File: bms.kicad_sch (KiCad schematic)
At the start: 95 parts, among them J1 Conn_01x13, J2 SWD, J3 I2C_IN, J4 I2C_OUT, SW1 SW_Push, U1 LMR51610, U2 STM32F103C8Tx, U3 MAX14920, U4 MAX11163, U5 MAX6126, U6 ADuM1252, Y1 8M

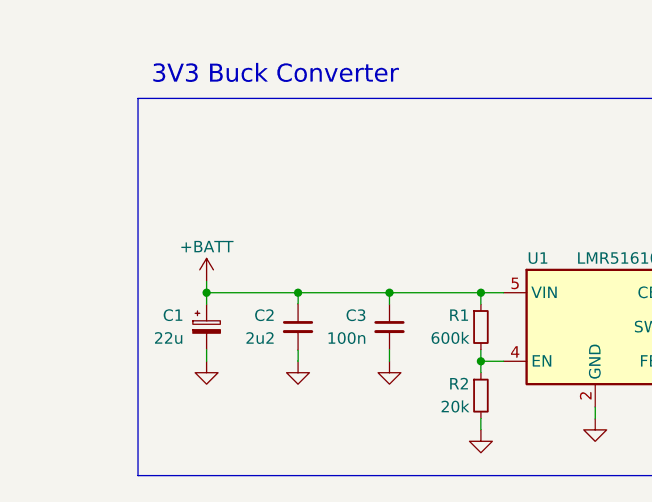
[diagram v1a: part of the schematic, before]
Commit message: schematic: Add input polyfuse
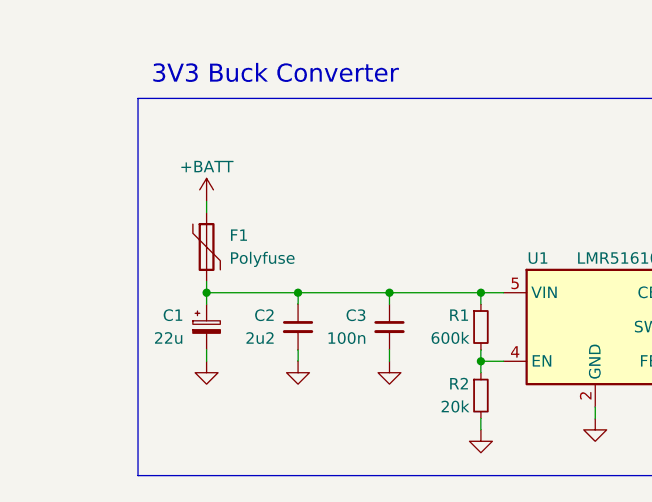
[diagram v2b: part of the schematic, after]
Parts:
- added F1: Polyfuse, Resistor_SMD:R_1206_3216Metric, symbol Device:Polyfuse
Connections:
- net +BATT: now also F1.1; no longer C1.1, C2.1, C3.1, R1.1, U1.5 (VIN)
- new net: C1.1, C2.1, C3.1, F1.2, R1.1, U1.5 (VIN)
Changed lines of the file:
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@@
 	(wire
 		(pts
+			(xy 33.02 35.56) (xy 33.02 36.83)
+		)
+		(stroke
+			(width 0)
+			(type default)
+		)
+	)
+	(wire
+		(pts
 			(xy 256.54 72.39) (xy 256.54 73.66)
 		)
@@
 	)
 	(symbol
+		(lib_id "Device:Polyfuse")
+		(at 33.02 40.64 0)
+		(unit 1)
+		(exclude_from_sim no)
+		(in_bom yes)
+		(on_board yes)
+		(dnp no)
+		(fields_autoplaced yes)
+		(property "Reference" "F1"
+			(at 35.56 39.3699 0)
+			(effects
+				(font
+					(size 1.27 1.27)
+				)
+				(justify left)
+			)
+		)
+		(property "Value" "Polyfuse"
+			(at 35.56 41.9099 0)
+			(effects
+				(font
+					(size 1.27 1.27)
+				)
+				(justify left)
+			)
+		)
+		(property "Footprint" "Resistor_SMD:R_1206_3216Metric"
+			(at 34.29 45.72 0)
+			(effects
+				(font
+					(size 1.27 1.27)
+				)
+				(justify left)
+				(hide yes)
+			)
+		)
+		(property "Datasheet" "~"
+			(at 33.02 40.64 0)
+			(effects
+				(font
+					(size 1.27 1.27)
+				)
+				(hide yes)
+			)
+		)
+		(property "Description" "Resettable fuse, polymeric positive temperature coefficient"
+			(at 33.02 40.64 0)
+			(effects
+				(font
+					(size 1.27 1.27)
+				)
+				(hide yes)
+			)
+		)
+		(property "Part Number" "1206L010/60WR"
+			(at 33.02 40.64 0)
+			(effects
+				(font
+					(size 1.27 1.27)
+				)
+				(hide yes)
+			)
+		)
+		(property "Role" "Input polyfuse"
+			(at 33.02 40.64 0)
+			(effects
+				(font
+					(size 1.27 1.27)
+				)
+				(hide yes)
+			)
+		)
+		(pin "1"
+		)
+		(pin "2"
+		)
+		(instances
+			(project ""
+				(path "/ae4a7653-8e6d-4e05-b144-1e5e3b2092b7"
+					(reference "F1")
+					(unit 1)
+				)
+			)
+		)
+	)
+	(symbol
 		(lib_id "power:GND")
 		(at 121.92 60.96 0)
@@
 	(symbol
 		(lib_id "power:+BATT")
-		(at 33.02 44.45 0)
+		(at 33.02 35.56 0)
 		(unit 1)
 		(exclude_from_sim no)
@@
 		(dnp no)
 		(property "Reference" "#PWR03"
-			(at 33.02 48.26 0)
+			(at 33.02 39.37 0)
 			(effects
 				(font
@@
 		)
 		(property "Value" "+BATT"
-			(at 33.02 40.64 0)
+			(at 33.02 31.75 0)
 			(effects
 				(font
@@
 		)
 		(property "Footprint" ""
-			(at 33.02 44.45 0)
+			(at 33.02 35.56 0)
 			(effects
 				(font
@@
 		)
 		(property "Datasheet" ""
-			(at 33.02 44.45 0)
+			(at 33.02 35.56 0)
 			(effects
 				(font
@@
 		)
 		(property "Description" "Power symbol creates a global label with name \"+BATT\""
-			(at 33.02 44.45 0)
+			(at 33.02 35.56 0)
 			(effects
 				(font

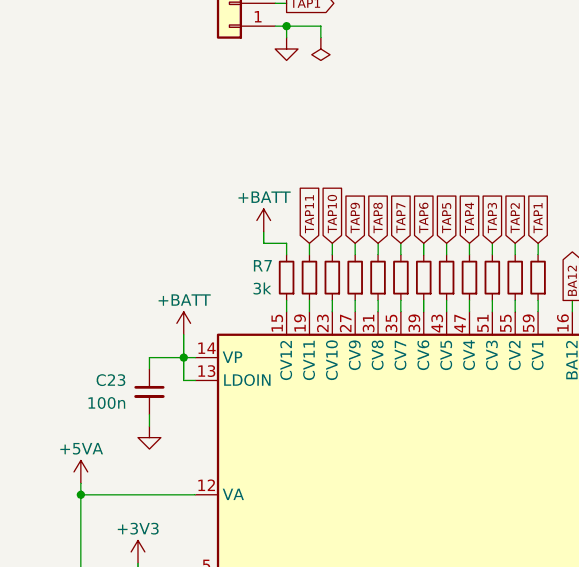
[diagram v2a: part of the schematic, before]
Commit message: schematic: Add resistor to MAX14920 input
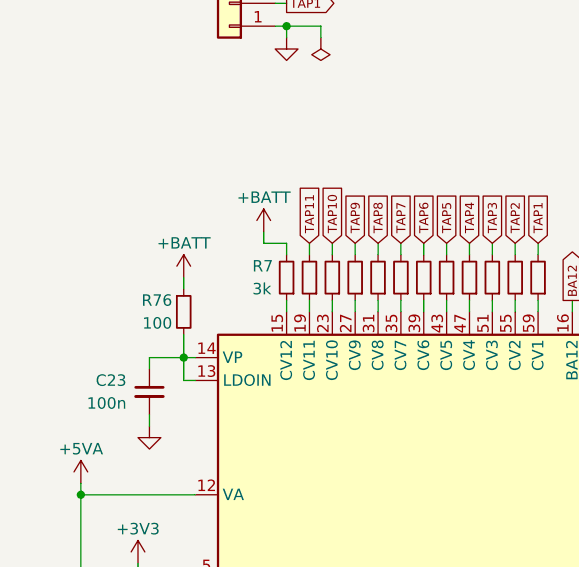
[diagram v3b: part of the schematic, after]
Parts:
- added R76: 100, Resistor_SMD:R_0603_1608Metric, symbol Device:R_Small
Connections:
- net +BATT: now also R76.1; no longer C23.1, U3.13 (LDOIN), U3.14 (VP)
- new net: C23.1, R76.2, U3.13 (LDOIN), U3.14 (VP)
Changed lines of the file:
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@@
 	(wire
 		(pts
+			(xy 30.48 137.16) (xy 30.48 138.43)
+		)
+		(stroke
+			(width 0)
+			(type default)
+		)
+	)
+	(wire
+		(pts
 			(xy 106.68 138.43) (xy 107.95 138.43)
 		)
@@
 	(symbol
 		(lib_id "power:+BATT")
-		(at 30.48 143.51 0)
+		(at 30.48 137.16 0)
 		(unit 1)
 		(exclude_from_sim no)
@@
 		(dnp no)
 		(property "Reference" "#PWR025"
-			(at 30.48 147.32 0)
+			(at 30.48 140.97 0)
 			(effects
 				(font
@@
 		)
 		(property "Value" "+BATT"
-			(at 30.48 139.7 0)
+			(at 30.48 133.35 0)
 			(effects
 				(font
@@
 		)
 		(property "Footprint" ""
-			(at 30.48 143.51 0)
+			(at 30.48 137.16 0)
 			(effects
 				(font
@@
 		)
 		(property "Datasheet" ""
-			(at 30.48 143.51 0)
+			(at 30.48 137.16 0)
 			(effects
 				(font
@@
 		)
 		(property "Description" "Power symbol creates a global label with name \"+BATT\""
-			(at 30.48 143.51 0)
+			(at 30.48 137.16 0)
 			(effects
 				(font
@@
 					(unit 1)
 				)
+			)
+		)
+	)
+	(symbol
+		(lib_id "Device:R_Small")
+		(at 30.48 140.97 0)
+		(unit 1)
+		(exclude_from_sim no)
+		(in_bom yes)
+		(on_board yes)
+		(dnp no)
+		(property "Reference" "R76"
+			(at 29.21 139.7 0)
+			(effects
+				(font
+					(size 1.27 1.27)
+				)
+				(justify right)
+			)
+		)
+		(property "Value" "100"
+			(at 29.21 142.24 0)
+			(effects
+				(font
+					(size 1.27 1.27)
+				)
+				(justify right)
+			)
+		)
+		(property "Footprint" "Resistor_SMD:R_0603_1608Metric"
+			(at 30.48 140.97 0)
+			(effects
+				(font
+					(size 1.27 1.27)
+				)
+				(hide yes)
+			)
+		)
+		(property "Datasheet" "~"
+			(at 30.48 140.97 0)
+			(effects
+				(font
+					(size 1.27 1.27)
+				)
+				(hide yes)
+			)
+		)
+		(property "Description" "Resistor, small symbol"
+			(at 30.48 140.97 0)
+			(effects
+				(font
+					(size 1.27 1.27)
+				)
+				(hide yes)
+			)
+		)
+		(property "Role" "MAX14920 inrush limit"
+			(at 30.48 140.97 0)
+			(effects
+				(font
+					(size 1.27 1.27)
+				)
+				(hide yes)
+			)
+		)
+		(pin "1"
+		)
+		(pin "2"
+		)
+		(instances
+			(project ""
+				(path "/ae4a7653-8e6d-4e05-b144-1e5e3b2092b7"
+					(reference "R76")
+					(unit 1)
+				)

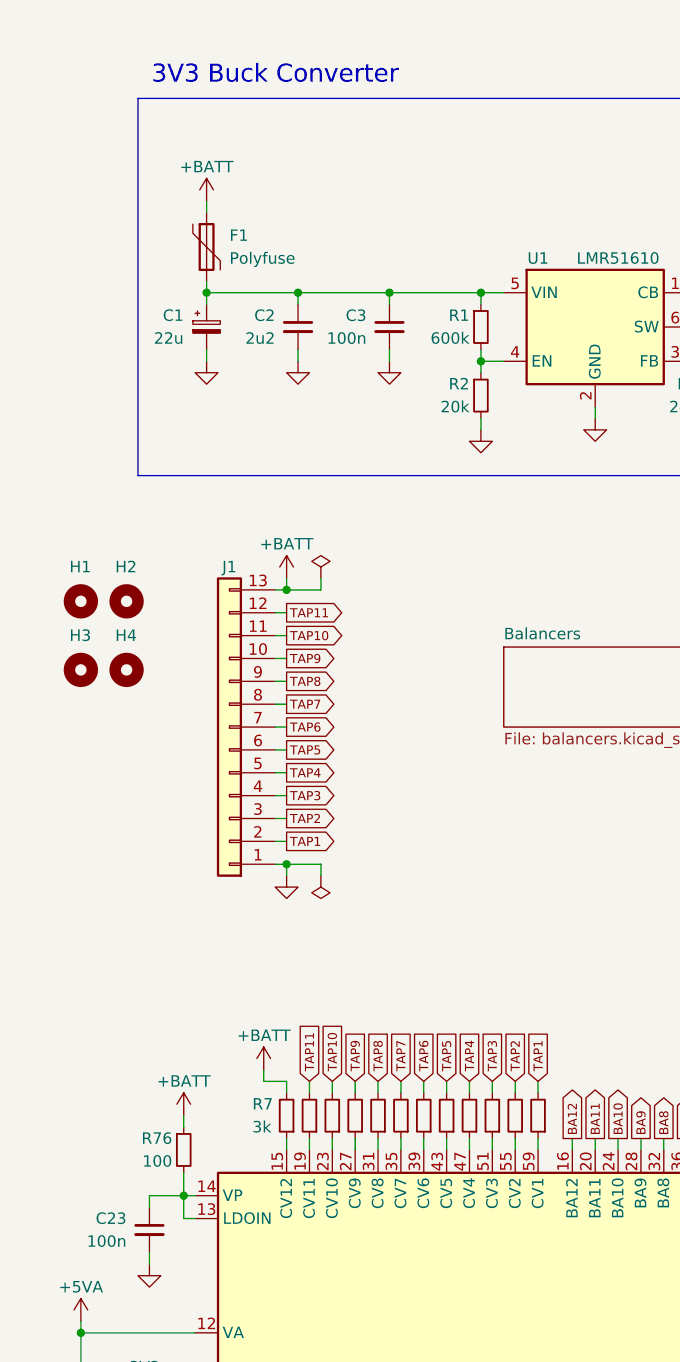
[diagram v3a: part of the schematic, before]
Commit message: schematic: Add some ferrite beads
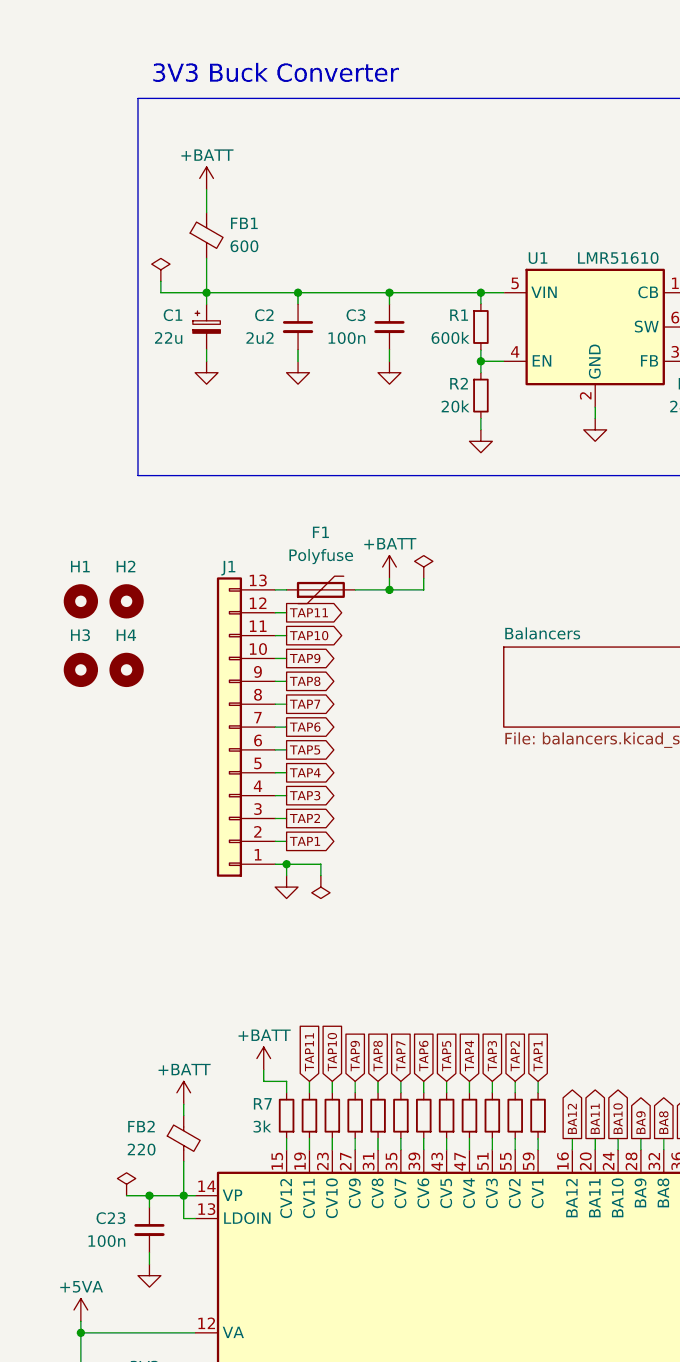
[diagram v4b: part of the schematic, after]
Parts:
- removed R76: 100, Resistor_SMD:R_0603_1608Metric, symbol Device:R_Small
- added FB1: 600, Inductor_SMD:L_0603_1608Metric, symbol Device:FerriteBead_Small
- added FB2: 220, Inductor_SMD:L_0603_1608Metric, symbol Device:FerriteBead_Small
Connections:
- net +BATT: now also F1.2, FB1.1, FB2.1; no longer F1.1, J1.13 (Pin_13)
- net at C1.1, C2.1, C3.1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: now also FB1.2; no longer F1.2
- net at C23.1, U3.13 (LDOIN), U3.14 (VP): now also FB2.2
- new net: F1.1, J1.13 (Pin_13)
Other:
- moved on the sheet: F1

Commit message: schematic: Assign remaining footprints
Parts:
- D13, D14, D15: footprint (none) -> Diode_SMD:D_SOD-323; Part Number (none) -> BZT52C3V6S
- J1: value Conn_01x13 -> CELL_TAPS; footprint (none) -> TerminalBlock_4Ucon:TerminalBlock_4Ucon_1x13_P3.50mm_Horizontal; Part Number (none) -> MX15EDGRC-3.5-13P-GN01-Cu-A
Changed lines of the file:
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@@
 			)
 		)
-		(property "Value" "Conn_01x13"
+		(property "Value" "CELL_TAPS"
 			(at 35.56 74.93 0)
 			(effects
@@
 			)
 		)
-		(property "Footprint" ""
+		(property "Footprint" "TerminalBlock_4Ucon:TerminalBlock_4Ucon_1x13_P3.50mm_Horizontal"
 			(at 35.56 93.98 0)
 			(effects
@@
 			)
 		)
-		(property "Part Number" ""
+		(property "Part Number" "MX15EDGRC-3.5-13P-GN01-Cu-A"
 			(at 35.56 93.98 0)
 			(effects
@@
 			)
 		)
-		(property "Footprint" ""
+		(property "Footprint" "Diode_SMD:D_SOD-323"
 			(at 110.49 138.43 90)
 			(effects
@@
 			)
 		)
+		(property "Part Number" "BZT52C3V6S"
+			(at 110.49 138.43 0)
+			(effects
+				(font
+					(size 1.27 1.27)
+				)
+				(hide yes)
+			)
+		)
 		(pin "1"
 		)
@@
 			)
 		)
-		(property "Footprint" ""
+		(property "Footprint" "Diode_SMD:D_SOD-323"
 			(at 125.73 138.43 90)
 			(effects
@@
 			)
 		)
+		(property "Part Number" "BZT52C3V6S"
+			(at 125.73 138.43 0)
+			(effects
+				(font
+					(size 1.27 1.27)
+				)
+				(hide yes)
+			)
+		)
 		(pin "1"
 		)
@@
 			)
 		)
-		(property "Footprint" ""
+		(property "Footprint" "Diode_SMD:D_SOD-323"
 			(at 140.97 138.43 90)
 			(effects
@@
 			(at 140.97 138.43 0)
 			(effects
+				(font
+					(size 1.27 1.27)
+				)
+				(hide yes)
+			)
+		)
+		(property "Part Number" "BZT52C3V6S"
+			(at 140.97 138.43 0)
+			(effects

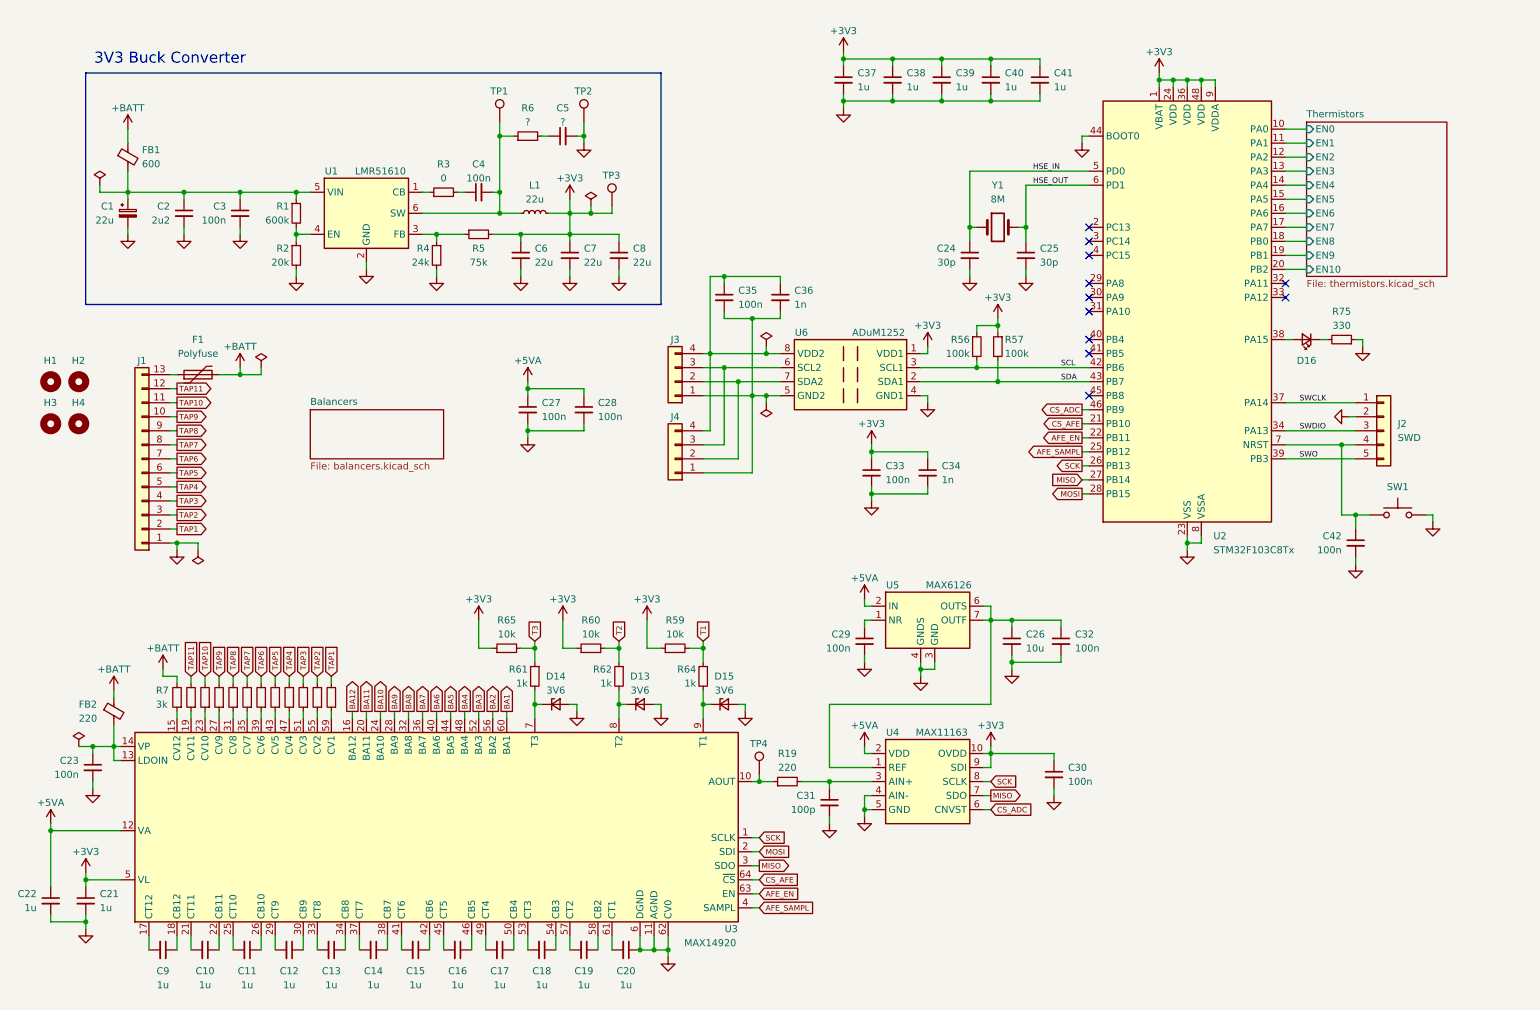
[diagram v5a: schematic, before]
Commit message: schematic: Add some more test points
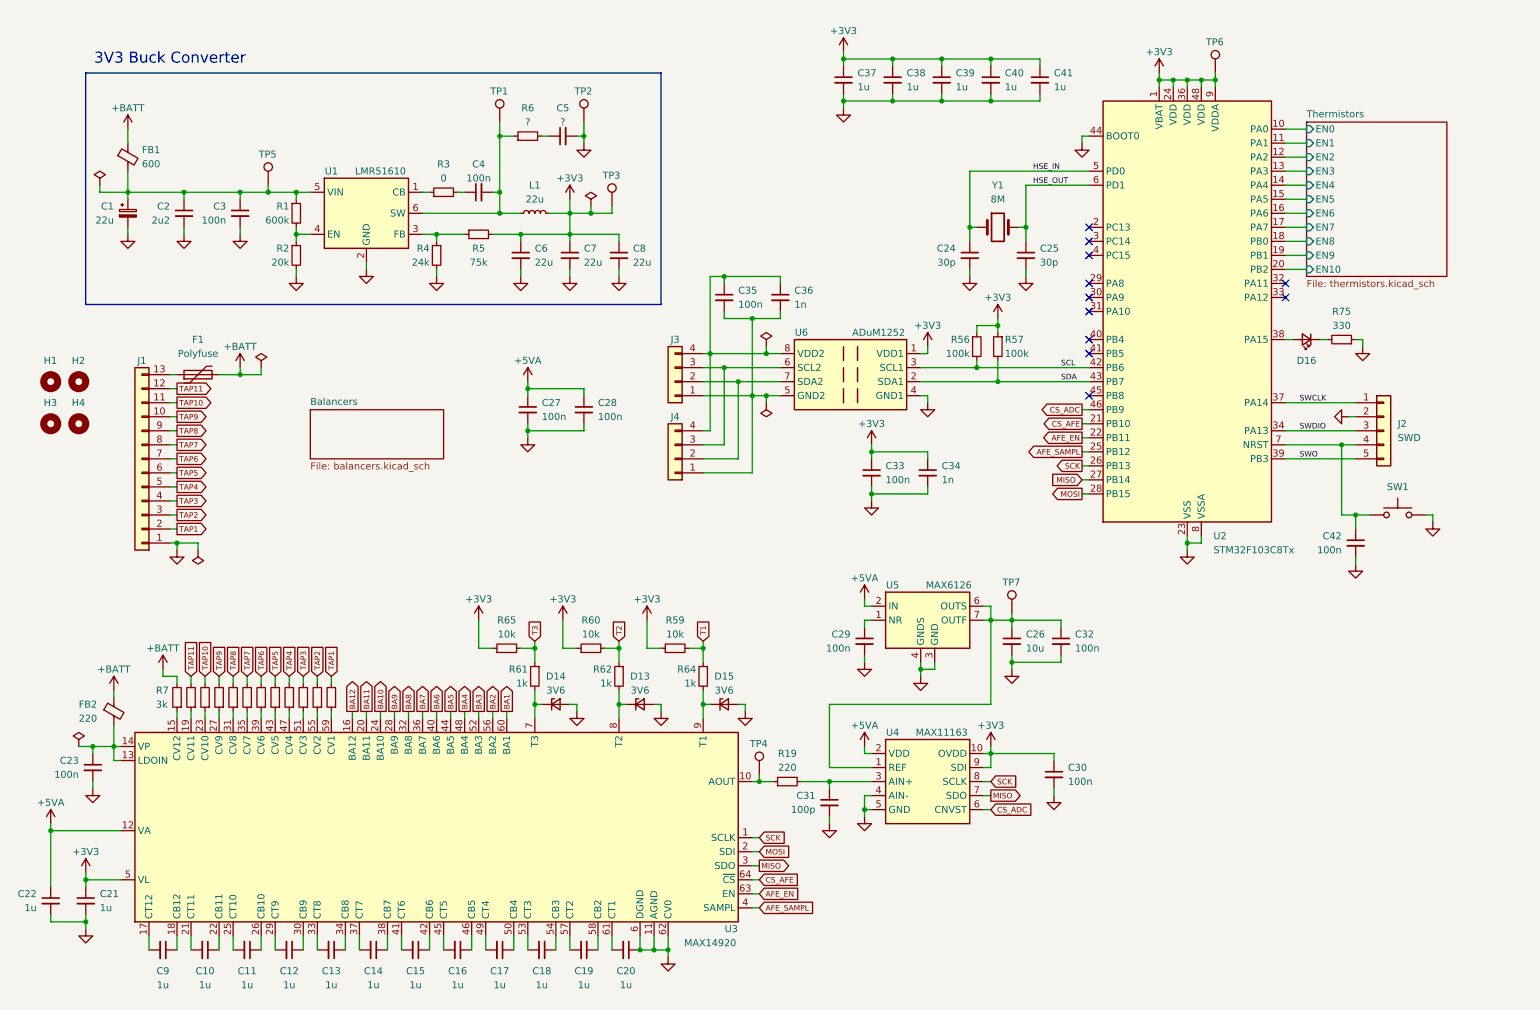
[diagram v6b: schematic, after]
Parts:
- added TP5, TP6, TP7: TestPoint, TestPoint:TestPoint_Keystone_5000-5004_Miniature, symbol Connector:TestPoint
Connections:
- net +3V3: now also TP6.1
- net at C26.1, C32.1, U4.1 (REF)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: now also TP7.1
- net at C1.1, C2.1, C3.1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: now also TP5.1
